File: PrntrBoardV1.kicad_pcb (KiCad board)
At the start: 4 copper layers, 99 x 99 mm, 215 parts, among them J1 EXT 5V, J10 Probe, J11 Extruder Heater, J12 Stepper, J13 Thermistor, J14 Max, J15 Min, J16 Max, J17 Min, J18 Max, J19 Min, J2 Bed Heater, J20 Stepper, J21 Stepper, J22 Stepper, J23 Stepper, J24 Probe, J25 Extruder Heater, J26 Stepper, J27 Thermistor, J28 Thermistor, J29 12-24V, J3 Z Probe, J30 Ext Motor Clock, J4 E0 Cool, J5 E0 Part, J6 E1 Cool, J7 E1 Part, J8 Always On Fan 1, J9 Always On Fan 2, U1 4078, U11 NUCLEO-64, U2 74HCT02, U3 74LVC125, U4 TMC5130, U5 TMC5130, U6 TMC5130, U7 TMC5130, U8 TMC5130

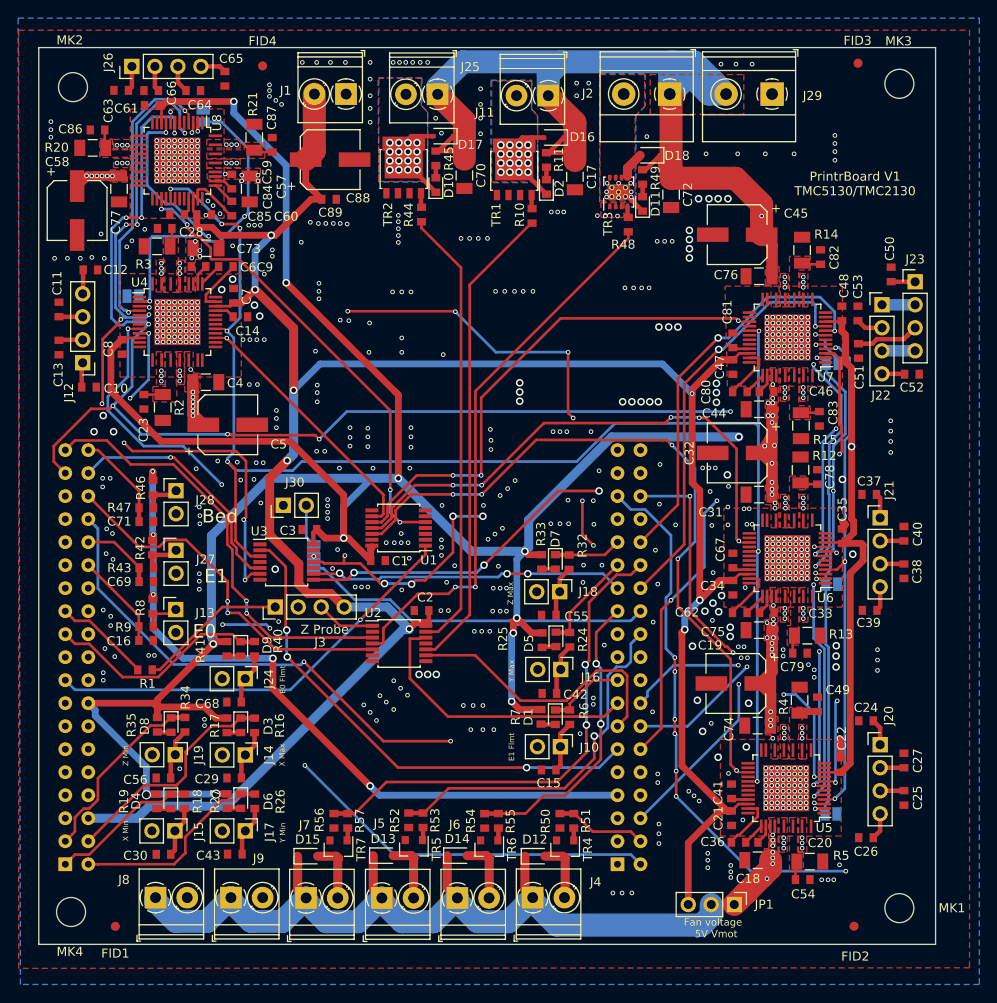
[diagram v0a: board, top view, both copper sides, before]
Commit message: Movet top FID to the top right corner. Added PCB origin. Switched 0.1uF 50V cpas to 0402 size.
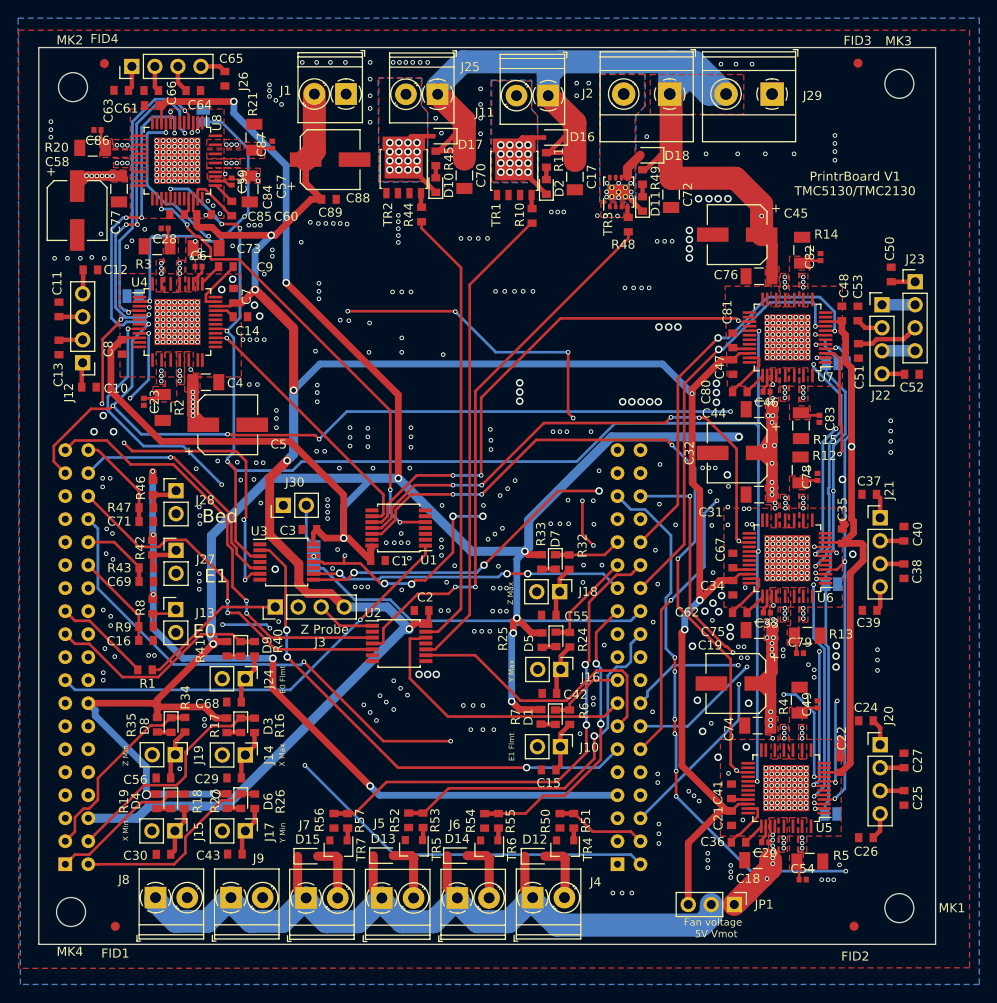
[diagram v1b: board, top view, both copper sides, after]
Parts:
- C20, C23, C28, C33, C46, C49, C54, C59, C6, C78, C79, C82, C83, C86, C87: footprint Capacitor_SMD:C_0603_1608Metric -> Capacitor_SMD:C_0402_1005Metric
- moved FID4 17.5 mm to (27.2, 20.8)

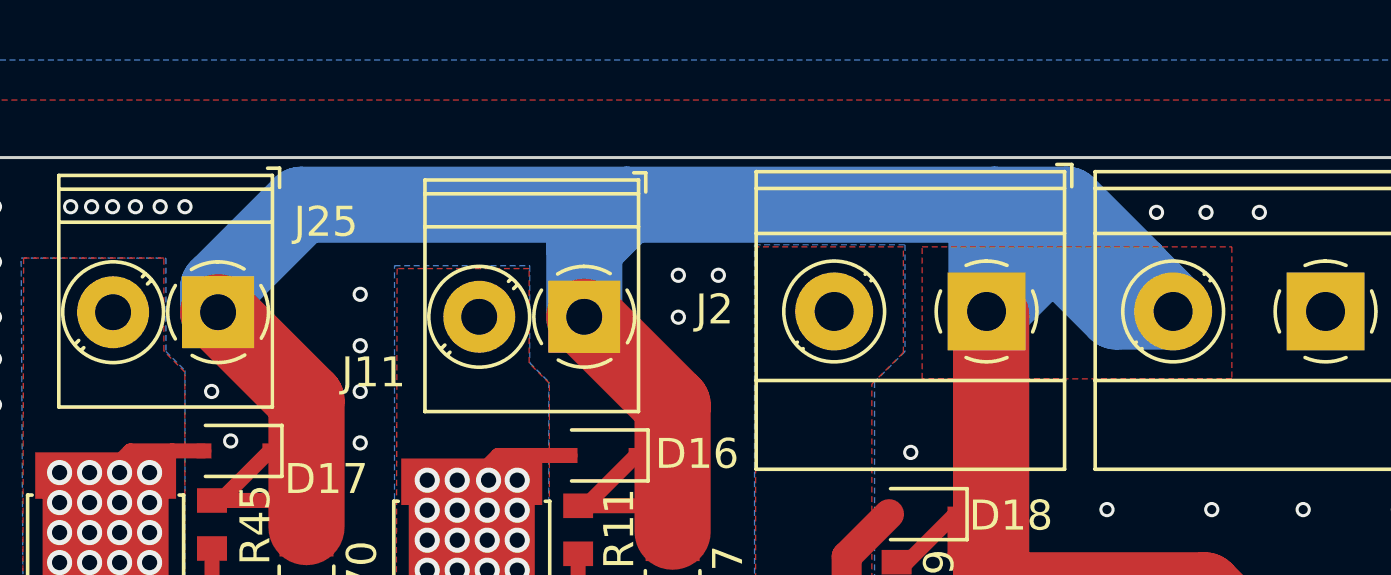
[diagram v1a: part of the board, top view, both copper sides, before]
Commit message: Added one more power trace for the top connectors.
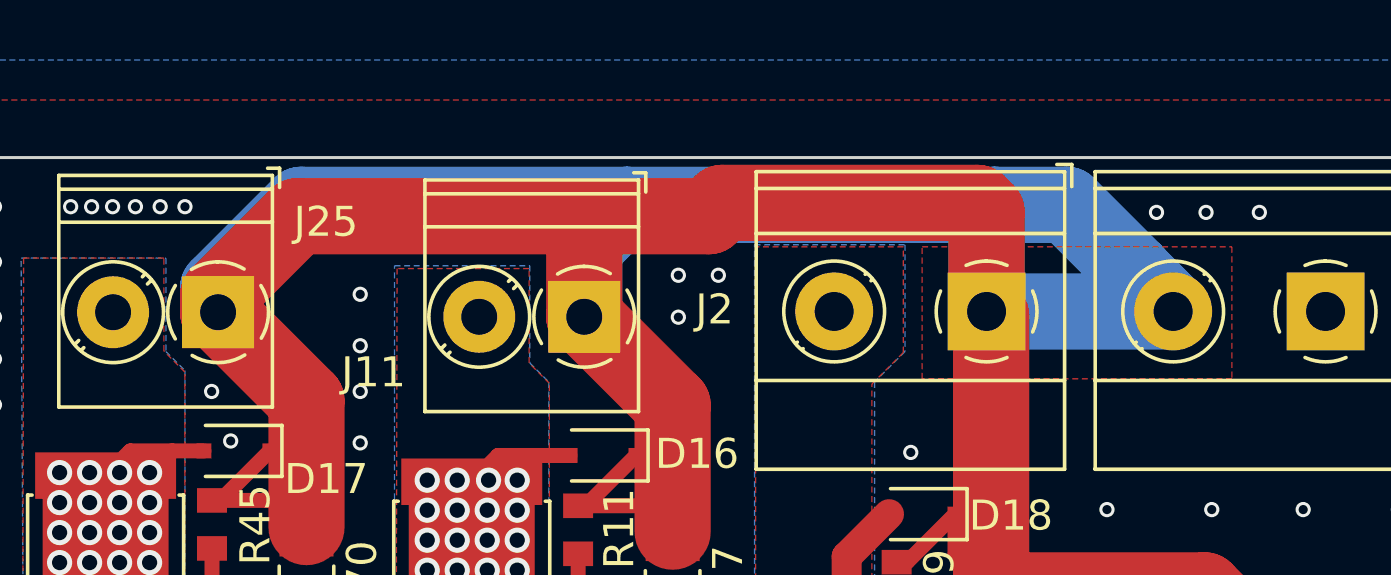
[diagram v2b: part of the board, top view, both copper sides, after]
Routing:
- net /V_MOTORS: track 264.5 -> 297.3 mm
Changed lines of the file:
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@@
     (thickness 1.6)
     (drawings 50)
-    (tracks 2522)
+    (tracks 2528)
     (zones 0)
     (modules 215)
@@
   )
   (setup
-    (last_trace_width 0.3)
+    (last_trace_width 2.54)
     (user_trace_width 0.1524)
     (user_trace_width 0.2032)
@@
   (segment (start 92.329 20.574) (end 89.916 20.574) (width 2.54) (layer B.Cu) (net 1))
   (segment (start 89.916 20.574) (end 77.6605 20.574) (width 2.54) (layer B.Cu) (net 1))
-  (segment (start 89.6493 24.13) (end 89.7255 24.13) (width 2.54) (layer B.Cu) (net 1))
-  (segment (start 89.7255 24.13) (end 91.567 22.2885) (width 2.54) (layer B.Cu) (net 1))
-  (segment (start 91.567 22.2885) (end 92.1385 22.2885) (width 2.54) (layer B.Cu) (net 1))
-  (segment (start 93.98 24.13) (end 95.8685 24.13) (width 2.54) (layer B.Cu) (net 1))
-  (segment (start 92.1385 22.2885) (end 93.98 24.13) (width 2.54) (layer B.Cu) (net 1))
   (segment (start 79.1845 31.4706) (end 79.1845 27.2542) (width 2.54) (layer F.Cu) (net 1))
   (segment (start 89.8017 33.4264) (end 96.9164 33.4264) (width 2.54) (layer F.Cu) (net 1))
@@
   (segment (start 66.091 30.4294) (end 66.9798 31.3182) (width 0.5) (layer F.Cu) (net 1))
   (segment (start 63.8302 30.4294) (end 66.091 30.4294) (width 0.5) (layer F.Cu) (net 1))
+  (segment (start 64.0334 24.1554) (end 64.0334 23.5966) (width 2.54) (layer F.Cu) (net 1))
+  (segment (start 64.0334 23.5966) (end 66.675 20.955) (width 2.54) (layer F.Cu) (net 1))
+  (segment (start 80.391 20.955) (end 80.8355 20.5105) (width 2.54) (layer F.Cu) (net 1))
+  (segment (start 80.8355 20.5105) (end 89.3445 20.5105) (width 2.54) (layer F.Cu) (net 1))
+  (segment (start 89.6493 20.8153) (end 89.6493 24.13) (width 2.54) (layer F.Cu) (net 1))
+  (segment (start 89.3445 20.5105) (end 89.6493 20.8153) (width 2.54) (layer F.Cu) (net 1))
+  (segment (start 76.2381 21.0566) (end 76.1365 20.955) (width 2.54) (layer F.Cu) (net 1))
+  (segment (start 76.2381 24.3078) (end 76.2381 21.0566) (width 2.54) (layer F.Cu) (net 1))
+  (segment (start 66.675 20.955) (end 76.1365 20.955) (width 2.54) (layer F.Cu) (net 1))
+  (segment (start 76.1365 20.955) (end 80.391 20.955) (width 2.54) (layer F.Cu) (net 1))
+  (segment (start 89.6493 24.13) (end 95.8685 24.13) (width 2.54) (layer B.Cu) (net 1))
   (segment (start 60.655029 31.800629) (end 60.655029 31.800629) (width 0.5) (layer F.Cu) (net 2))
   (segment (start 63.8302 34.9758) (end 61.6044 32.75) (width 0.5) (layer F.Cu) (net 2))

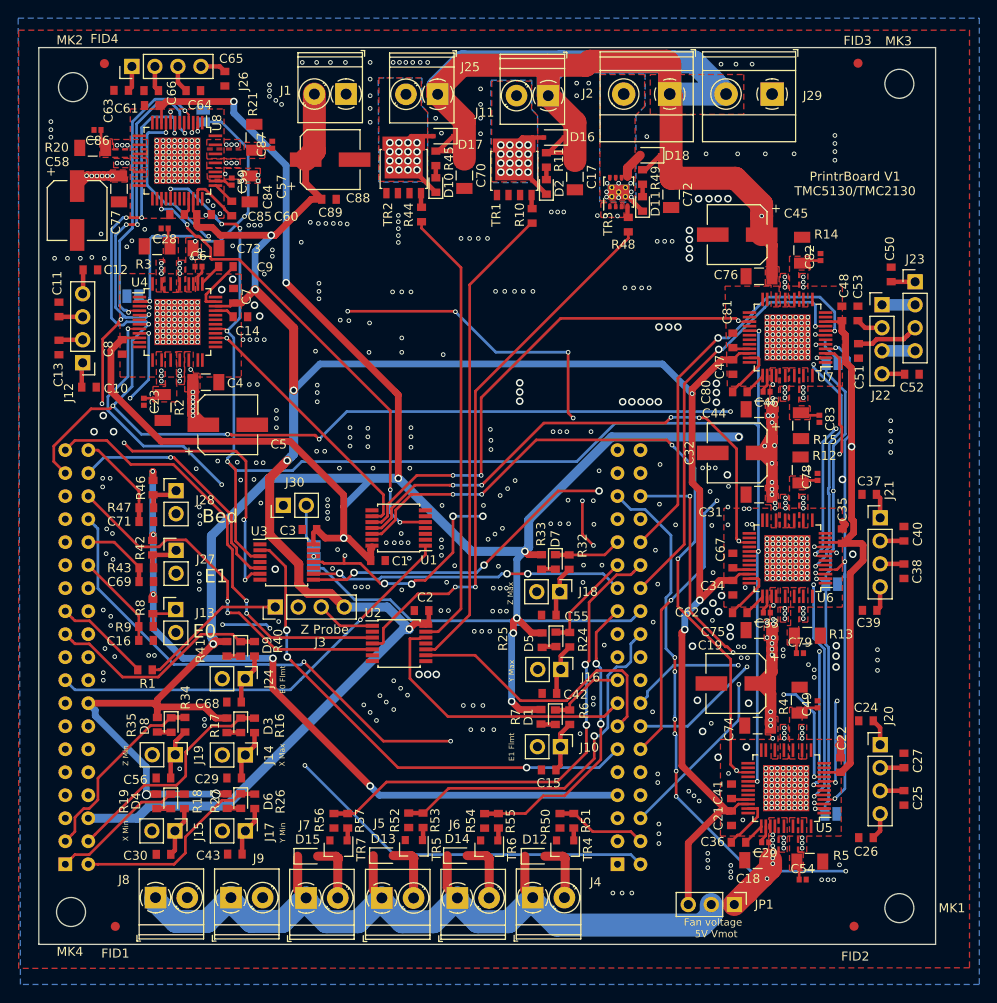
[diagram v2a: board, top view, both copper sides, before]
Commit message: Updated TR3 foor print and re-routed tracks.
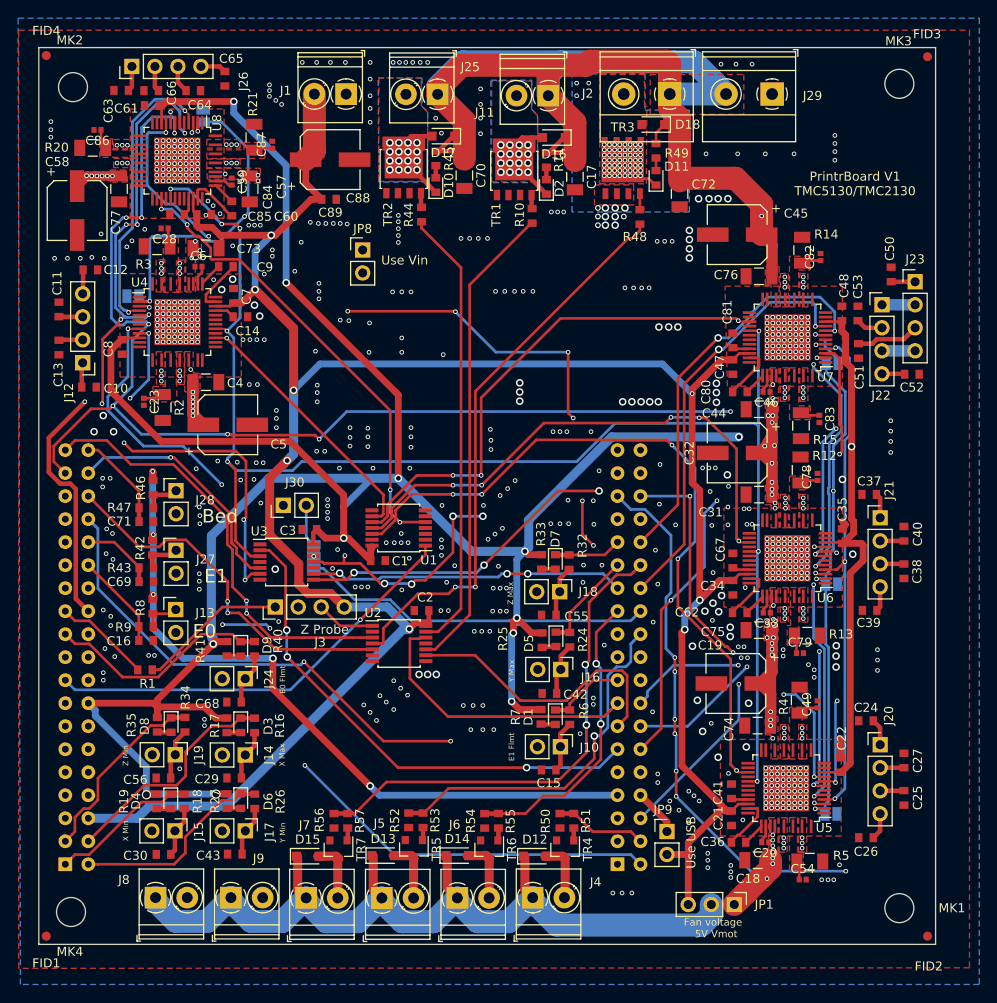
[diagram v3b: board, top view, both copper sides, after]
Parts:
- added JP8: Use VIn, Connector_PinHeader_2.54mm:PinHeader_1x02_P2.54mm_Vertical, F.Cu at (55.8, 41.3)
- added JP9: Use USB, Connector_PinHeader_2.54mm:PinHeader_1x02_P2.54mm_Vertical, F.Cu at (89.3, 105.5)
- C89: value 0.001uF -> 1000pF
- D12, D13, D14, D15, D16, D17, D18: footprint Diode_SMD:D_SOD-323F -> Diode_SMD:D_SOD-323_HandSoldering
- TR3: footprint PrntrBoardV1:Texas_S-PVSON-N8_ThermalVias -> PrntrBoardV1:PG-TDSON-8-FL
- moved FID2 8.18 mm to (118.1, 117.1)
- moved FID3 7.70 mm to (118.1, 20.0)
- moved FID1 7.70 mm to (20.8, 117.1)
- moved FID4 6.47 mm to (20.8, 19.9)
- moved D18 3.41 mm to (87.8, 27.5)
- moved R49 3.25 mm to (88.1, 30.4)
- moved D11 3.24 mm to (88.1, 33.4)
- moved TR3 2.69 mm to (84.5, 32.3), turned to 0 degrees
- moved R48 1.54 mm to (86.4, 37.7)
- moved C72 0.94 mm to (90.7, 35.1)
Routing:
- net Net-(JP8-Pad2): track 0.00 -> 78.8 mm, vias 0 -> 2
- net /V_MOTORS: track 297.3 -> 303.8 mm
- net /VBUS: track 0.00 -> 5.21 mm
- net /Heated Bed/HEATER: track 5.46 -> 2.14 mm, vias 13 -> 56
- net /5V: track 270.1 -> 272.5 mm
- net /Heated Bed/PWM: track 61.1 -> 62.7 mm
- net GND: vias 670 -> 678
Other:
- board text added: "Use USB"
- board text added: "Use Vin"

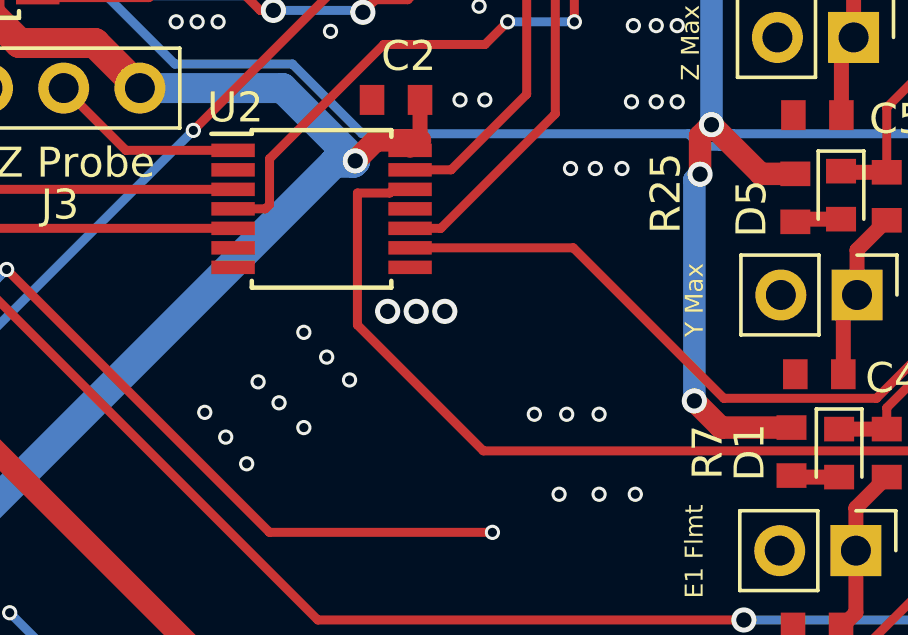
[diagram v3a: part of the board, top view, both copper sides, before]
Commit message: Added 10k pullups to control inputs for heaters, to disable heaters when control module is not installed.
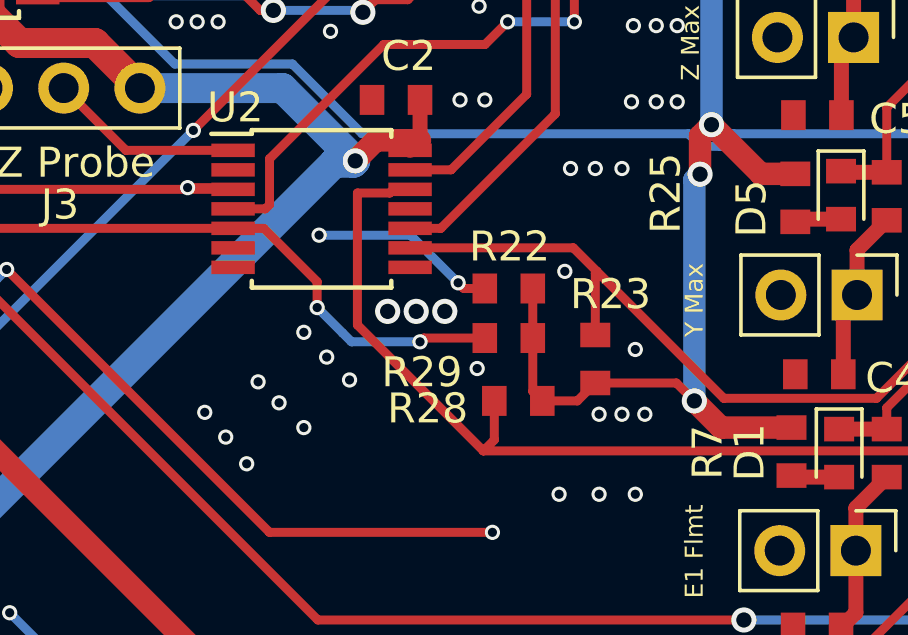
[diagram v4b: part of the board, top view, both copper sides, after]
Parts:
- added R22: 10k, Resistor_SMD:R_0603_1608Metric, F.Cu at (66.0, 87.4)
- added R23: 10k, Resistor_SMD:R_0603_1608Metric, F.Cu at (68.9, 89.8)
- added R28: 10k, Resistor_SMD:R_0603_1608Metric, F.Cu at (66.3, 91.2)
- added R29: 10k, Resistor_SMD:R_0603_1608Metric, F.Cu at (66.0, 89.1)
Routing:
- net /Z_PROBE_MOD: track 48.2 -> 61.1 mm, vias 2 -> 5
- net /BED_PWM_IN: track 41.0 -> 51.6 mm, vias 2 -> 4
- net /3.3V: track 358.1 -> 367.5 mm
- net /E0_PWM_IN: track 31.9 -> 34.1 mm
- net /E1_PWM_IN: track 31.5 -> 33.3 mm
- net GND: vias 678 -> 681
